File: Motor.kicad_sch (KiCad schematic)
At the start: 34 parts, among them U1 MCF8315C1VQRGFRQ1

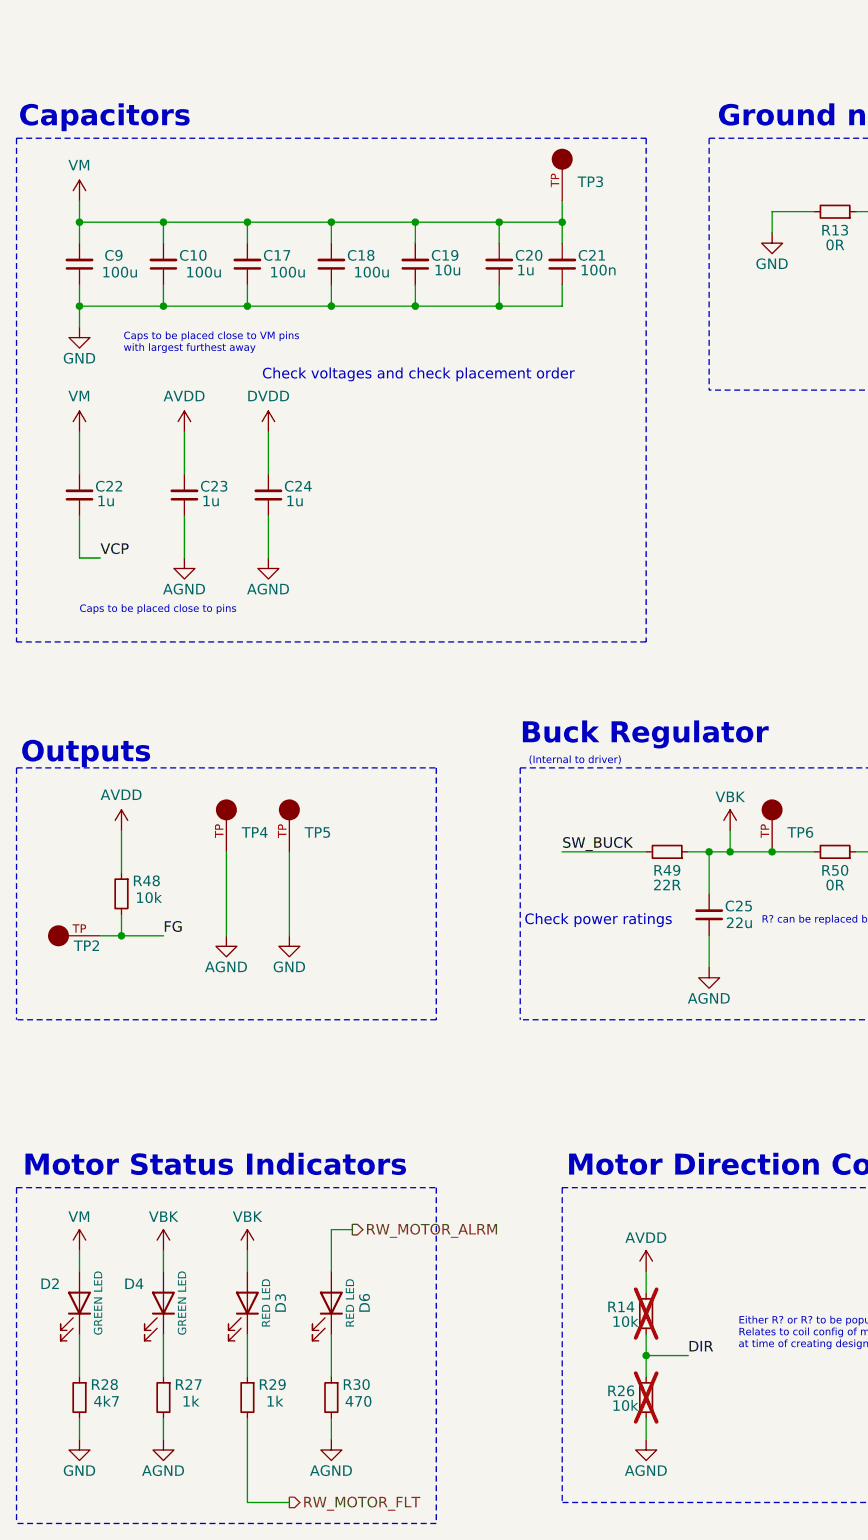
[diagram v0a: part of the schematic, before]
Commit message: Checked all power and voltage ratings and corrected where needed. Still need footprints and layout completed.
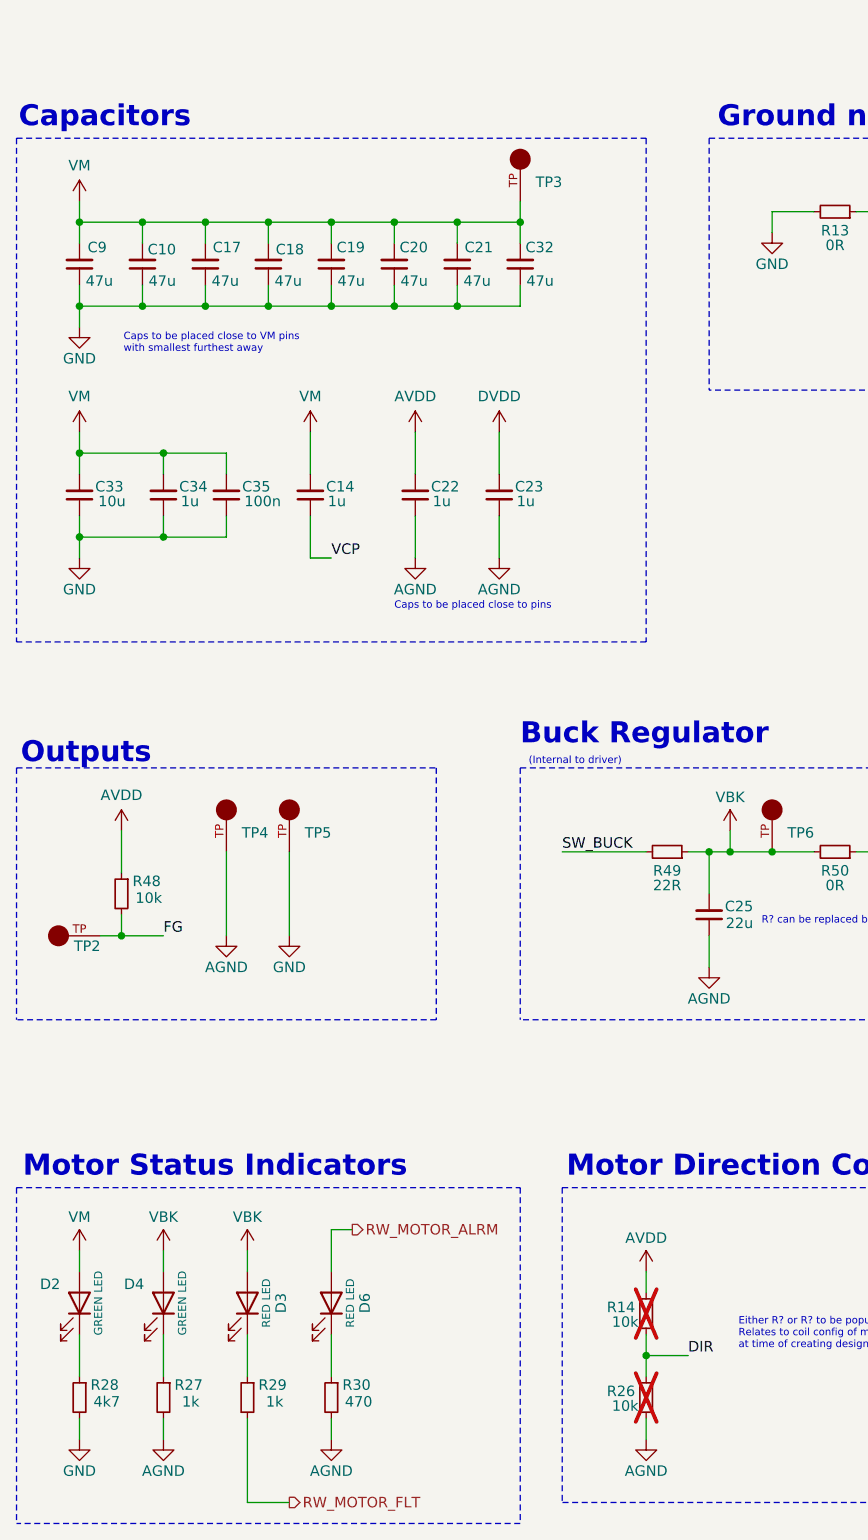
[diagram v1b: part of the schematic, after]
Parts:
- removed C24: 1u, Capacitor_SMD:C_0603_1608Metric, symbol Device:C_Small
- added C14, C34: 1u, Capacitor_SMD:C_0603_1608Metric, symbol Device:C_Small
- added C32: 47u, Capacitor_SMD:C_1206_3216Metric_Pad1.33x1.80mm_HandSolder, symbol Device:C_Small
- added C33: 10u, Capacitor_SMD:C_1206_3216Metric_Pad1.33x1.80mm_HandSolder, symbol Device:C_Small
- added C35: 100n, Capacitor_SMD:C_0402_1005Metric_Pad0.74x0.62mm_HandSolder, symbol Device:C_Small
- C10, C17, C18, C9: value 100u -> 47u; footprint Capacitor_SMD:C_0603_1608Metric -> Capacitor_SMD:C_1206_3216Metric_Pad1.33x1.80mm_HandSolder; Digikey (none) -> https://www.digikey.com/en/products/detail/tdk-corporation/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; Part (none) -> C3216X5R1E476M160AC
- C19: value 10u -> 47u; footprint Capacitor_SMD:C_0603_1608Metric -> Capacitor_SMD:C_1206_3216Metric_Pad1.33x1.80mm_HandSolder; Digikey (none) -> https://www.digikey.com/en/products/detail/tdk-corporation/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; Part (none) -> C3216X5R1E476M160AC
- C20: value 1u -> 47u; footprint Capacitor_SMD:C_0603_1608Metric -> Capacitor_SMD:C_1206_3216Metric_Pad1.33x1.80mm_HandSolder; Digikey (none) -> https://www.digikey.com/en/products/detail/tdk-corporation/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; Part (none) -> C3216X5R1E476M160AC
- C21: value 100n -> 47u; footprint Capacitor_SMD:C_0603_1608Metric -> Capacitor_SMD:C_1206_3216Metric_Pad1.33x1.80mm_HandSolder; Digikey (none) -> https://www.digikey.com/en/products/detail/tdk-corporation/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; Part (none) -> C3216X5R1E476M160AC
- C22, C23: Digikey (none) -> https://www.digikey.com/en/products/detail/samsung-electro-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; Part (none) -> CL10B105KA8NNNC
- C8: Digikey (none) -> https://www.digikey.com/en/products/detail/murata-electroni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; Part (none) -> GCM188R71H473KA55D
- D3, D6: Flight LTST-C190KGKT -> LTST-C190KRKT; Manufacturer_Part_Number LTST-C190KGKT -> LTST-C190KRKT; Proto LTST-C190KGKT -> LTST-C190KRKT
- R13, R50: footprint Resistor_SMD:R_0603_1608Metric -> Resistor_SMD:R_0805_2012Metric_Pad1.20x1.40mm_HandSolder
- R49: footprint Resistor_SMD:R_0603_1608Metric -> Resistor_SMD:R_2512_6332Metric_Pad1.40x3.35mm_HandSolder; Digikey (none) -> https://www.digikey.com/en/products/detail/vishay-dale/CRCW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; Part (none) -> CRCW251222R0FKEGHP
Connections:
- net AGND: now also C22.1
- net AVDD: now also C22.2; no longer C23.2
- net DVDD: now also C23.2
- net GND: now also C32.1, C33.1, C34.1, C35.1
- net VCP: now also C14.1; no longer C22.1
- net VM: now also C14.2, C32.2, C33.2, C34.2, C35.2; no longer C22.2
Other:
- note added: "Caps to be placed close to VM pins with smallest furthest away"
- note removed: "Caps to be placed close to VM pins with largest furthest away"
- note removed: "Check power ratings"
- note removed: "Check voltages and check placement order"
- moved on the sheet: TP3

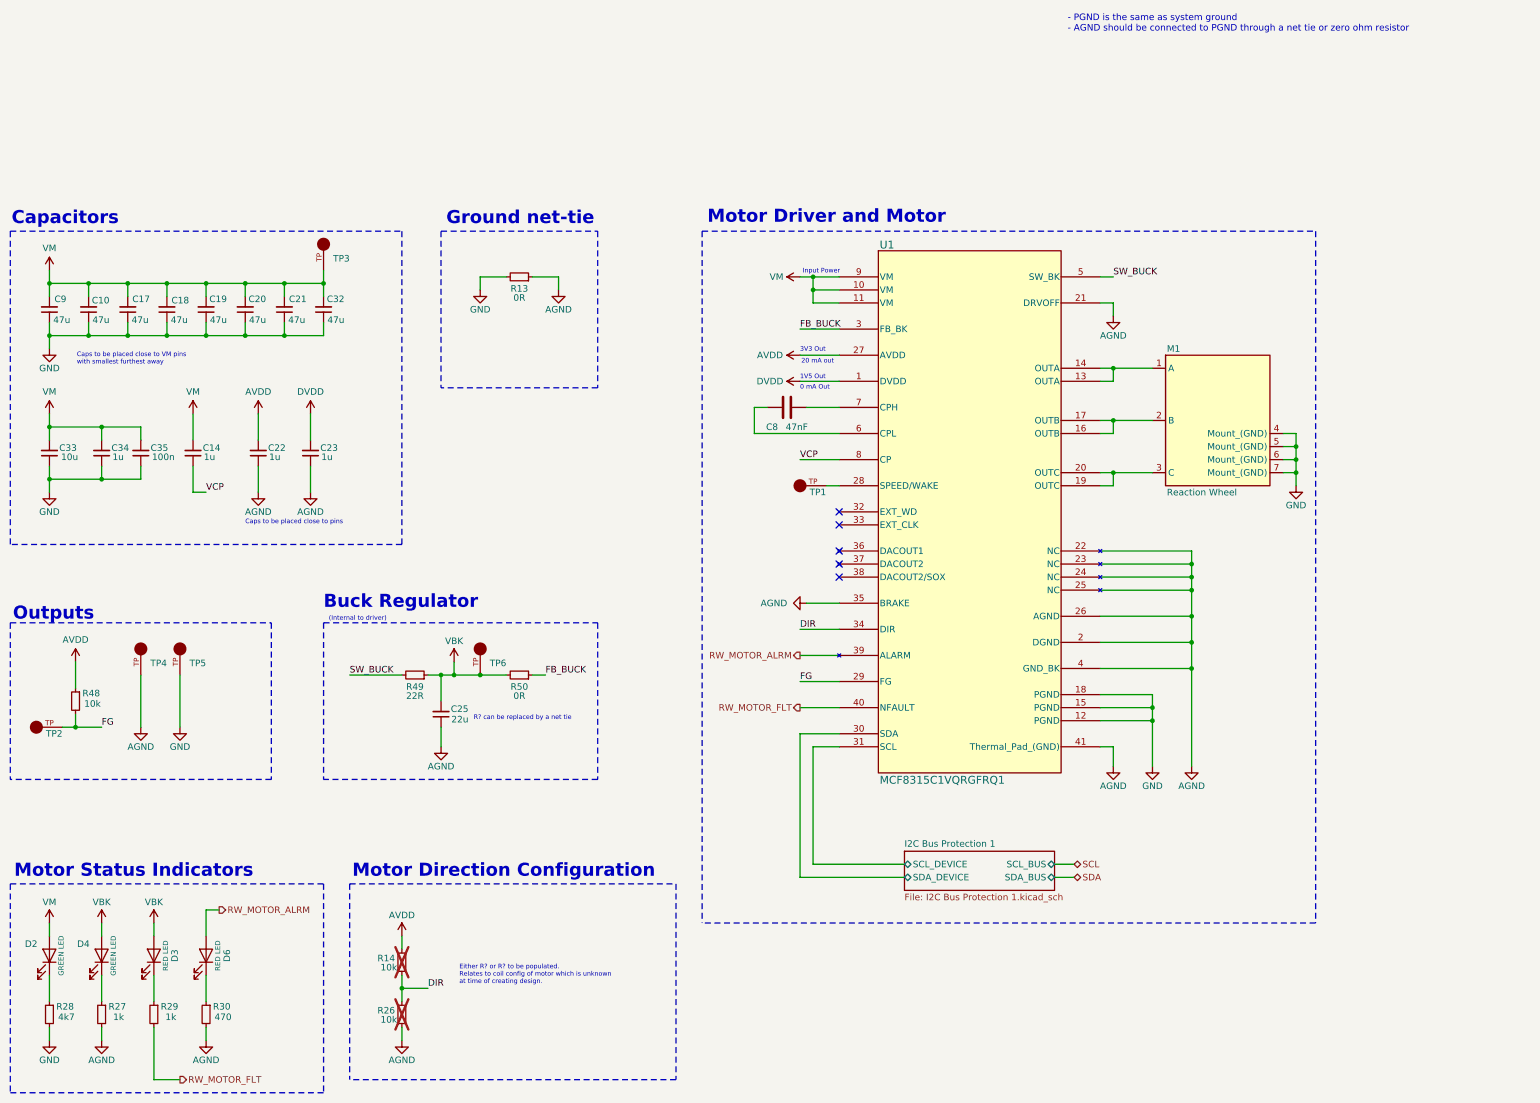
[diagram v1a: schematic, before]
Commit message: Add more test points
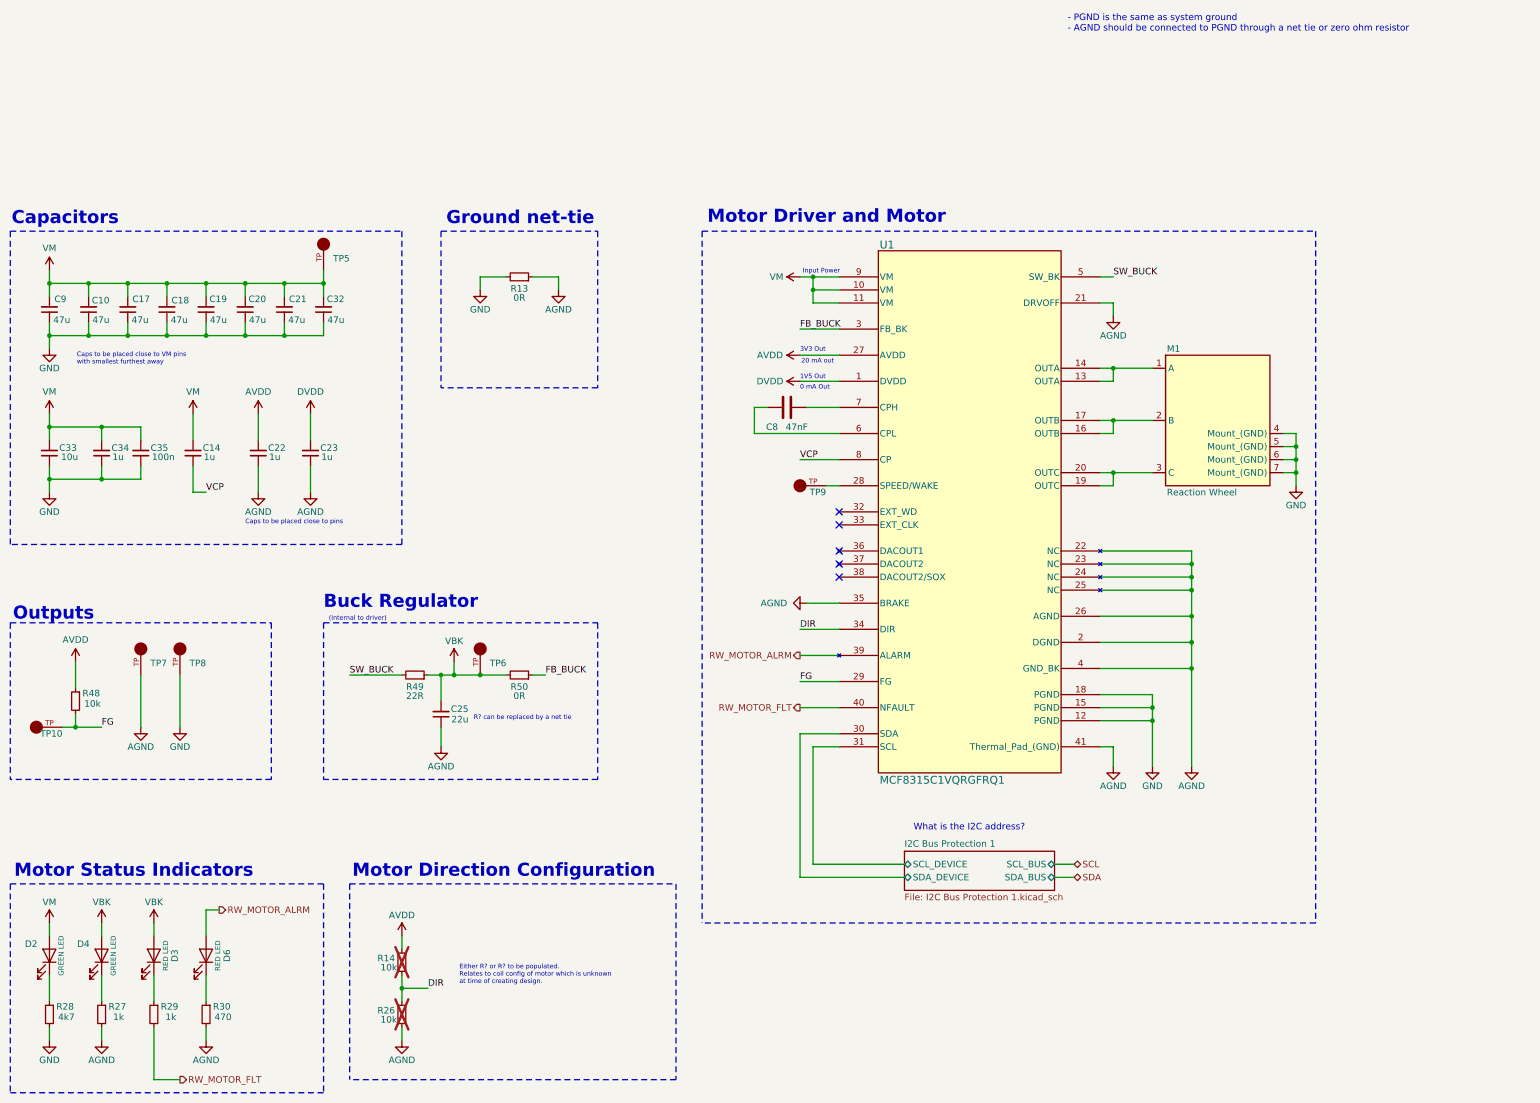
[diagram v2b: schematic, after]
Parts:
- renumbered TP2 to TP10, TP3 to TP5, TP4 to TP7, TP5 to TP8, TP1 to TP9
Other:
- note added: "What is the I2C address?"
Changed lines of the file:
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@@
 		)
 	)
+	(text "What is the I2C address?"
+		(exclude_from_sim no)
+		(at 201.168 140.716 0)
+		(effects
+			(font
+				(size 1.27 1.27)
+				(color 255 0 0 1)
+			)
+			(justify left top)
+		)
+	)
 	(text "Motor Driver and Motor"
 		(exclude_from_sim no)
@@
 		(on_board yes)
 		(dnp no)
-		(property "Reference" "TP3"
+		(property "Reference" "TP5"
 			(at 91.44 29.972 90)
 			(do_not_autoplace yes)
@@
 			(project "Avionics-RWboard"
 				(path "/833dc880-24c2-430b-8cf7-cc984eb87a9d/6fe6dcb0-4022-4a1b-8f5d-25ced07893ae"
-					(reference "TP3")
+					(reference "TP5")
 					(unit 1)
 				)
@@
 		(on_board yes)
 		(dnp no)
-		(property "Reference" "TP4"
+		(property "Reference" "TP7"
 			(at 55.88 108.712 90)
 			(do_not_autoplace yes)
@@
 			(project "Avionics-RWboard"
 				(path "/833dc880-24c2-430b-8cf7-cc984eb87a9d/6fe6dcb0-4022-4a1b-8f5d-25ced07893ae"
-					(reference "TP4")
+					(reference "TP7")
 					(unit 1)
 				)
@@
 		(on_board yes)
 		(dnp no)
-		(property "Reference" "TP5"
+		(property "Reference" "TP8"
 			(at 63.5 108.712 90)
 			(do_not_autoplace yes)
@@
 			(project "Avionics-RWboard"
 				(path "/833dc880-24c2-430b-8cf7-cc984eb87a9d/6fe6dcb0-4022-4a1b-8f5d-25ced07893ae"
-					(reference "TP5")
+					(reference "TP8")
 					(unit 1)
 				)
@@
 		(on_board yes)
 		(dnp no)
-		(property "Reference" "TP1"
+		(property "Reference" "TP9"
 			(at 184.15 75.438 0)
 			(do_not_autoplace yes)
@@
 			(project ""
 				(path "/833dc880-24c2-430b-8cf7-cc984eb87a9d/6fe6dcb0-4022-4a1b-8f5d-25ced07893ae"
-					(reference "TP1")
+					(reference "TP9")
 					(unit 1)
 				)
@@
 		(on_board yes)
 		(dnp no)
-		(property "Reference" "TP2"
+		(property "Reference" "TP10"
 			(at 35.56 122.428 0)
 			(do_not_autoplace yes)
@@
 			(project "Avionics-RWboard"
 				(path "/833dc880-24c2-430b-8cf7-cc984eb87a9d/6fe6dcb0-4022-4a1b-8f5d-25ced07893ae"
-					(reference "TP2")
+					(reference "TP10")
 					(unit 1)
 				)

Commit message: Layout mostly complete
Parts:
- added R54, R55, R58: 0R, Resistor_SMD:R_0402_1005Metric_Pad0.72x0.64mm_HandSolder, symbol Device:R_Small
- M1: footprint (none) -> Argus_RW_Library:Reaction_Wheel
- R14, R26: value 10k -> 0R; footprint Resistor_SMD:R_0603_1608Metric -> Resistor_SMD:R_0402_1005Metric_Pad0.72x0.64mm_HandSolder
- TP10, TP5, TP6, TP7, TP8, TP9: footprint (none) -> Argus_RW_Library:KEYSTONE_5001
- U1: footprint VQFN40_RGF_TEX -> Argus_RW_Library:VQFN40_RGF_TEX
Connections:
- net AGND: now also R54.1, R55.1, R58.1; no longer R26.1, U1.21 (DRVOFF), U1.35 (BRAKE)
- net AVDD: now also R26.2
- net DIR: now also R54.2; no longer R26.2
- new net: R58.2, U1.21 (DRVOFF)
- new net BRAKE: R26.1, R55.2, U1.35 (BRAKE)
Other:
- note added: "I2C address: 0x60"
- note added: "Motor Configuration"
- note removed: "Either R? or R? to be populated. Relates to coil config of motor which is unknown at time of creating design."
- note removed: "Motor Direction Configuration"
- note removed: "What is the I2C address?"
- title: (none) -> Argus Reaction Wheel
- moved on the sheet: C25, R13, R49, R50
